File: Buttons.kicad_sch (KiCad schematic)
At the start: 0 parts

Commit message: added buttons schematic
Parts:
- added C27, C28, C29, C30, C31, C32, C33, C34: 100nF, 0_capacitors:C_0402_1005Metric, symbol 0_capacitors:CL05B104KO5NNNC
- added R20, R23, R25, R27, R29, R31, R33, R35: 47kΩ, 0_resistors:R_0402_1005Metric, symbol 0_resistors:0402WGF4702TCE
- added R21, R22, R24, R26, R28, R30, R32, R34: 5.1kΩ, 0_resistors:R_0402_1005Metric, symbol 0_resistors:0402WGF5101TCE
- added S1, S2: SKRTLAE010, 0_switches:SKRTLAE010, symbol 0_switches:SKRTLAE010
- added SW1, SW2, SW3, SW4, SW5, SW6: Button SPST SMD Tactile Switch, 0_switches:SW_TS-1088-AR02016, symbol 0_switches:SW_Push
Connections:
- new net: C31.1, R28.2, R29.2, SW5.1
- new net: C33.1, R32.2, R33.2, S1.2
- new net: C34.1, R34.2, R35.2, S2.2
- new net: C32.1, R30.2, R31.2, SW6.1
- new net: C29.1, R24.2, R25.2, SW3.1
- new net: C27.1, R20.2, R21.2, SW1.2
- new net: C28.1, R22.2, R23.2, SW2.1
- new net: C30.1, R26.2, R27.2, SW4.1
- new net +3.3V: R20.1, R23.1, R25.1, R27.1, R29.1, R31.1, R33.1, R35.1
- new net BUTTON1: R21.1
- new net BUTTON2: R22.1
- new net BUTTON3: R24.1
- new net BUTTON4: R26.1
- new net BUTTON5: R28.1
- new net BUTTON6: R30.1
- new net BUTTON7: R32.1
- new net BUTTON8: R34.1
- new net GND: C27.2, C28.2, C29.2, C30.2, C31.2, C32.2, C33.2, C34.2, S1.1, S1.3, S2.1, S2.3, SW1.1, SW2.2, SW3.2, SW4.2, SW5.2, SW6.2
- no-connect marks 0 -> 4
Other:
- title: (none) -> UI - Buttons

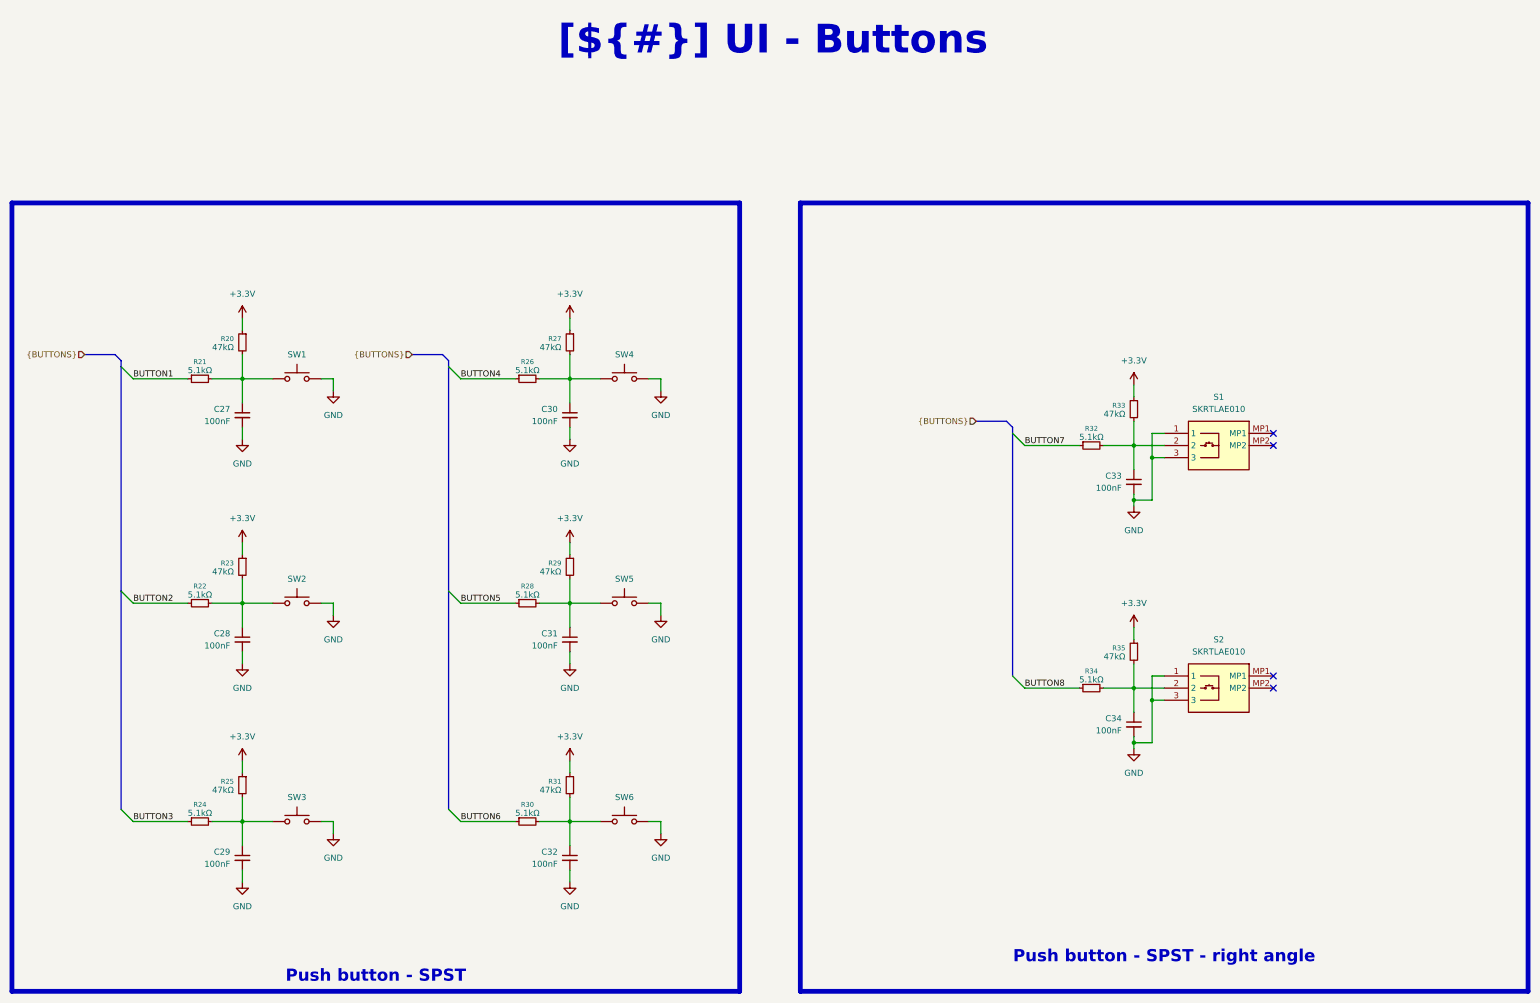
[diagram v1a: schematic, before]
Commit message: 3 pos toggle switch input
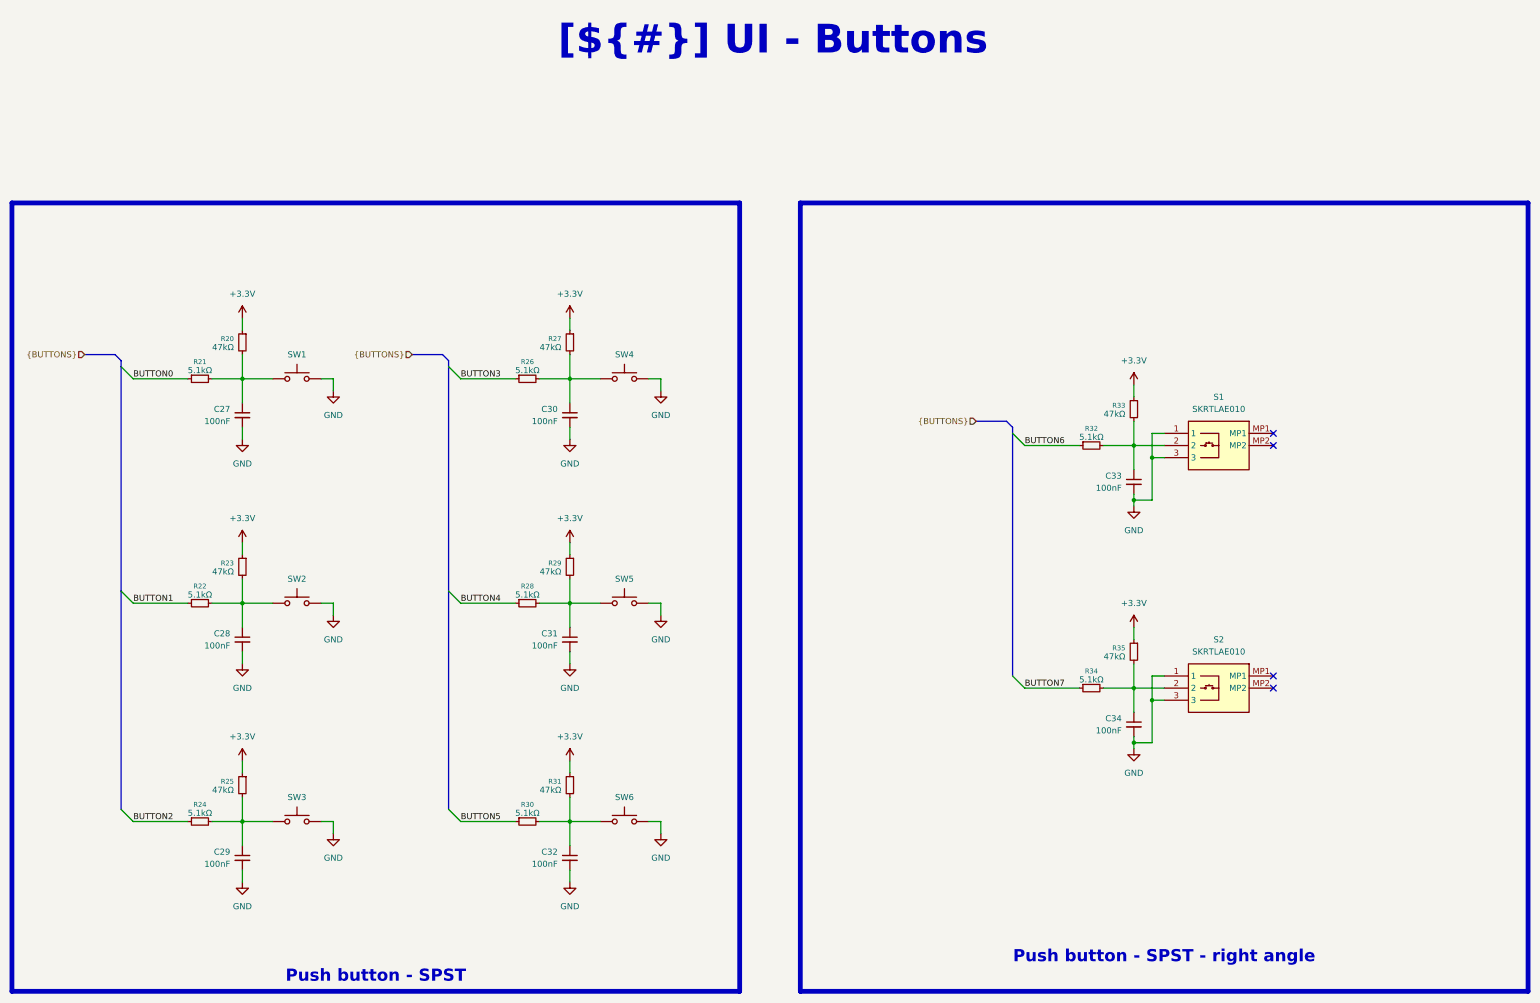
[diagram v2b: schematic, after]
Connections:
- net BUTTON8 is gone; now on net BUTTON7: R34.1
- net BUTTON1: now also R22.1; no longer R21.1
- net BUTTON2: now also R24.1; no longer R22.1
- net BUTTON3: now also R26.1; no longer R24.1
- net BUTTON4: now also R28.1; no longer R26.1
- net BUTTON5: now also R30.1; no longer R28.1
- net BUTTON6: now also R32.1; no longer R30.1
- net BUTTON7: no longer R32.1
- new net BUTTON0: R21.1
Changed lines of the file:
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@@
 	)
 	(bus_alias "BUTTONS"
-		(members "BUTTON[1..8]")
+		(members "BUTTON[0..7]" "TOGGLE[0..1]")
 	)
 	(rectangle
@@
 		)
 	)
-	(label "BUTTON8"
+	(label "BUTTON7"
 		(at 262.89 154.94 0)
 		(effects
@@
 		)
 	)
-	(label "BUTTON6"
+	(label "BUTTON5"
 		(at 144.78 182.88 0)
 		(effects
@@
 		)
 	)
-	(label "BUTTON2"
+	(label "BUTTON1"
 		(at 76.2 137.16 0)
 		(effects
@@
 		)
 	)
-	(label "BUTTON7"
+	(label "BUTTON6"
 		(at 262.89 104.14 0)
 		(effects
@@
 		)
 	)
-	(label "BUTTON1"
+	(label "BUTTON0"
 		(at 76.2 90.17 0)
 		(effects
@@
 		)
 	)
-	(label "BUTTON4"
+	(label "BUTTON3"
 		(at 144.78 90.17 0)
 		(effects
@@
 		)
 	)
-	(label "BUTTON5"
+	(label "BUTTON4"
 		(at 144.78 137.16 0)
 		(effects
@@
 		)
 	)
-	(label "BUTTON3"
+	(label "BUTTON2"
 		(at 76.2 182.88 0)
 		(effects

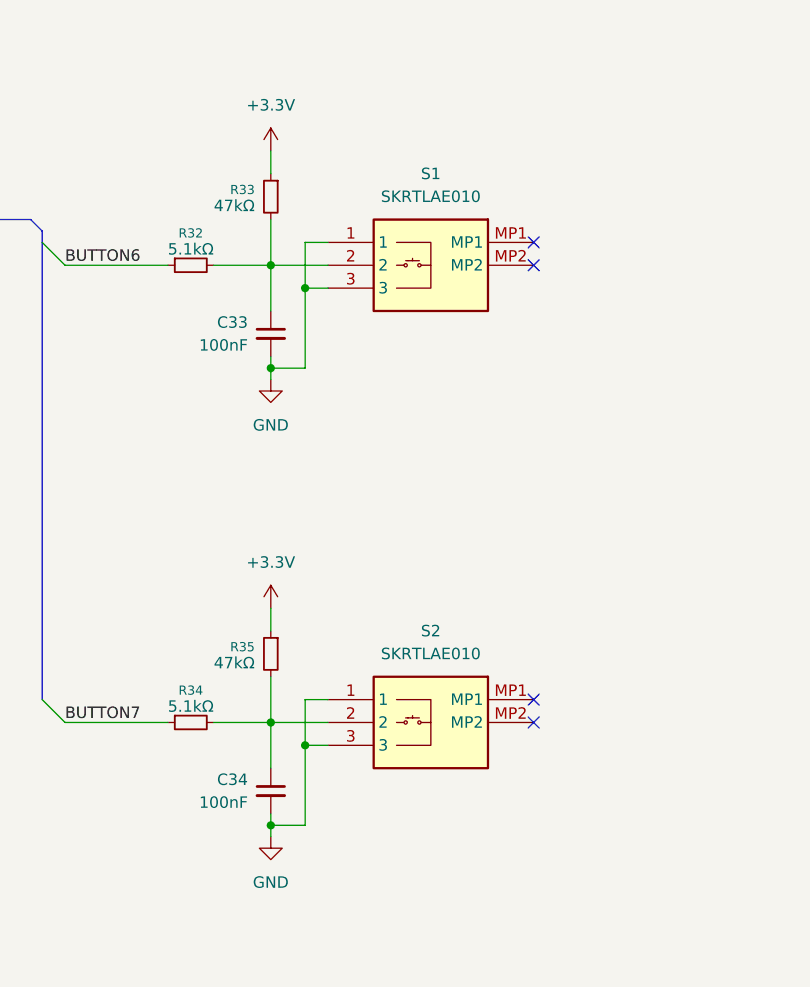
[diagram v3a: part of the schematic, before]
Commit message: change buttons footprints to 2pin 2.0mm connectors
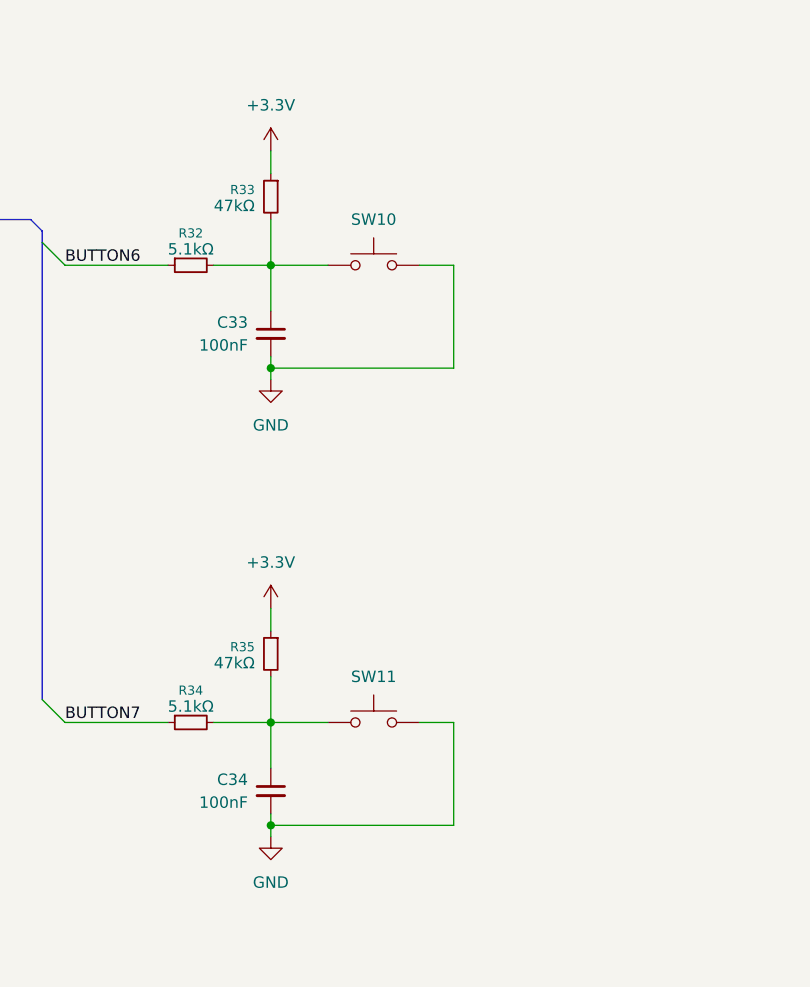
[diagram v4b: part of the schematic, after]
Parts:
- removed S1, S2: SKRTLAE010, 0_switches:SKRTLAE010, symbol 0_switches:SKRTLAE010
- added SW10, SW11: Button SPST SMD Tactile Switch, Connector_JST:JST_PH_B2B-PH-K_1x02_P2.00mm_Vertical, symbol 0_switches:SW_Push
- SW1, SW2, SW3, SW4, SW5, SW6: footprint 0_switches:SW_TS-1088-AR02016 -> Connector_JST:JST_PH_B2B-PH-K_1x02_P2.00mm_Vertical; Supplier Part Number 1 C720477 -> C131337
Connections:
- net GND: now also SW10.2, SW11.2
- net at C33.1, R32.2, R33.2: now also SW10.1
- net at C34.1, R34.2, R35.2: now also SW11.1
- no-connect marks 4 -> 0

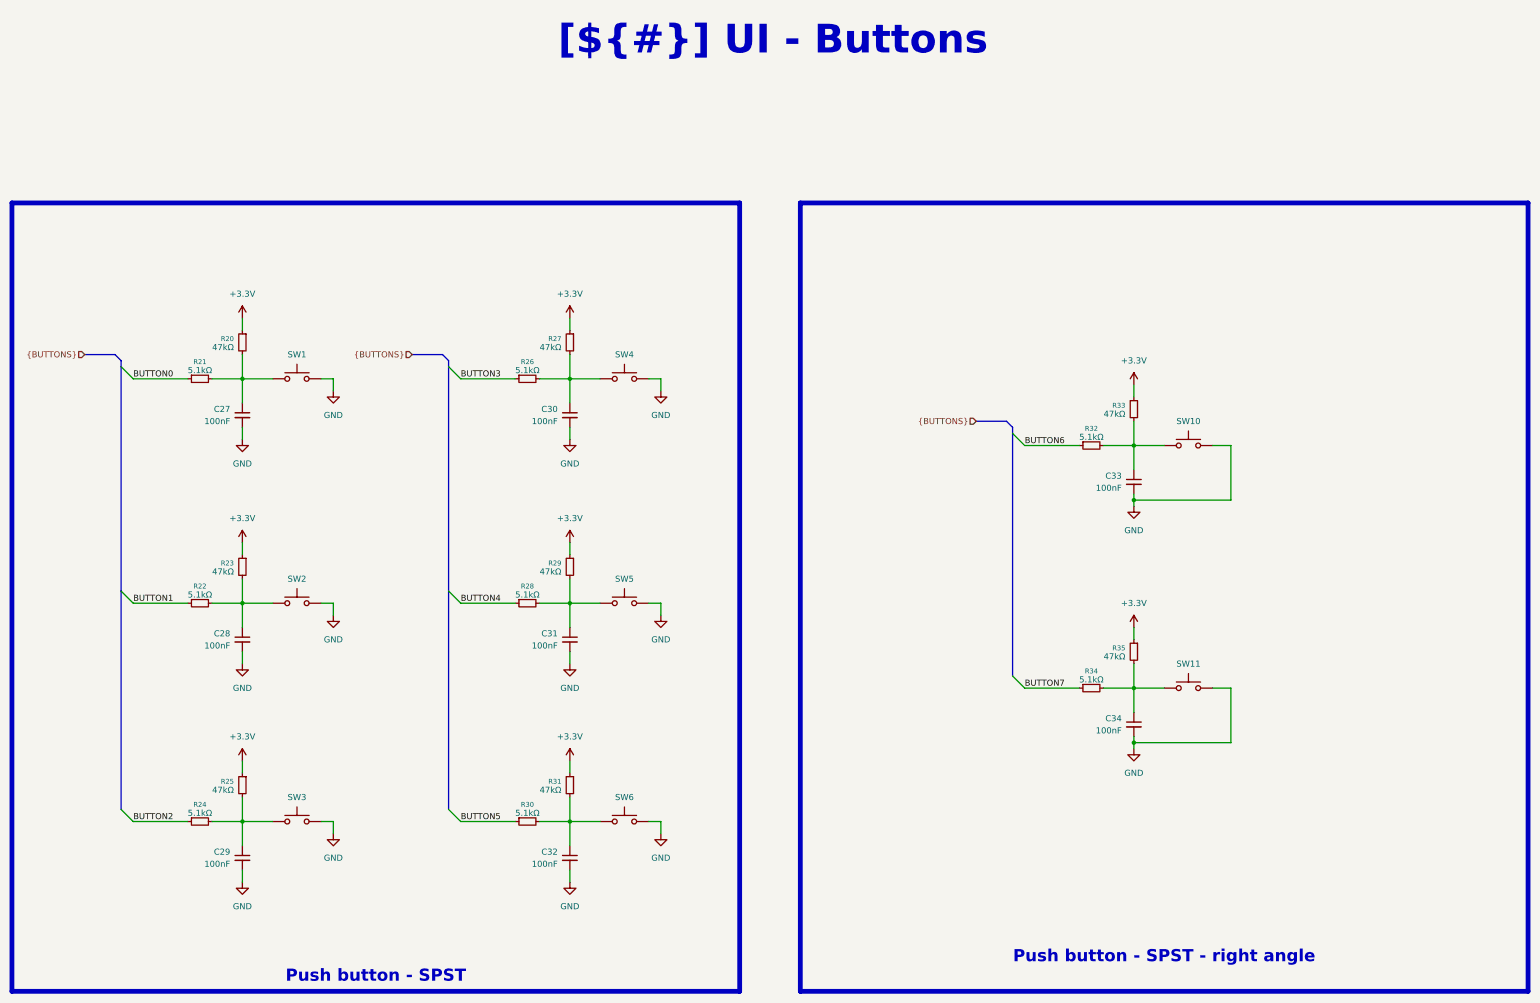
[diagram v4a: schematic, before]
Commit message: added tvs diodes to protect inputs + final component placement
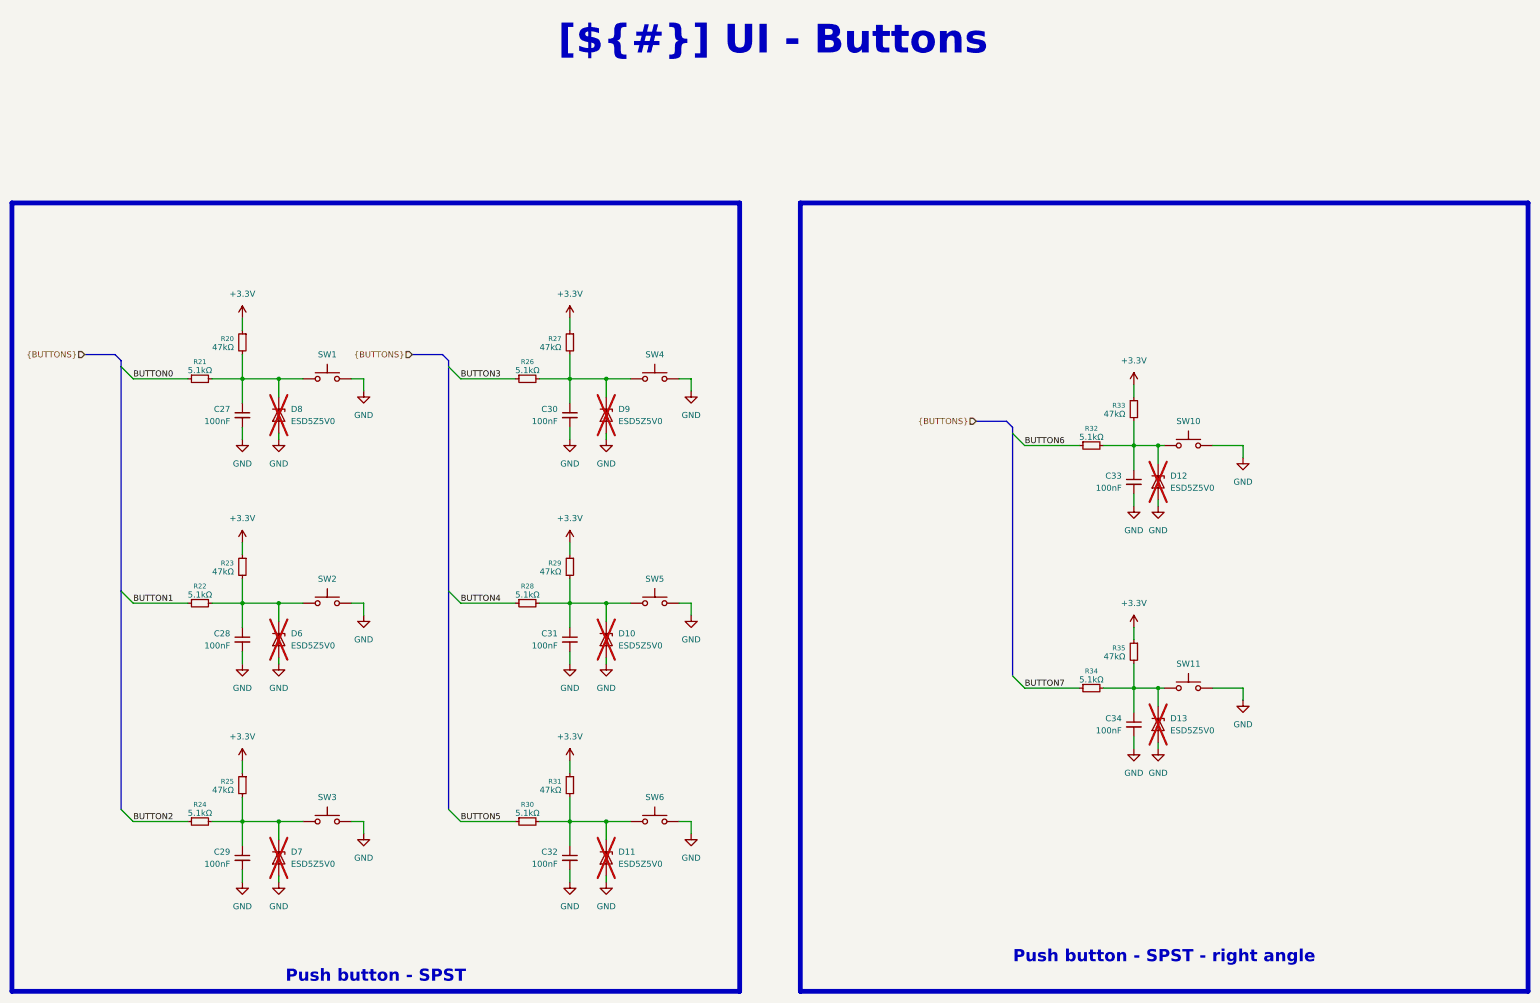
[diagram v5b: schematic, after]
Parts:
- added D10, D11, D12, D13, D6, D7, D8, D9: ESD5Z5V0, 0_diodes:D_SOD-523, symbol 0_diodes:ESD5Z5V0
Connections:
- net GND: now also SW1.2, D10.2 (A), D11.2 (A), D12.2 (A), D13.2 (A), D6.2 (A), D7.2 (A), D8.2 (A), D9.2 (A); no longer SW1.1
- net at C31.1, R28.2, R29.2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: now also D10.1 (K)
- net at C33.1, R32.2, R33.2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: now also D12.1 (K)
- net at C34.1, R34.2, R35.2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: now also D13.1 (K)
- net at C32.1, R30.2, R31.2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: now also D11.1 (K)
- net at C29.1, R24.2, R25.2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: now also D7.1 (K)
- net at C27.1, R20.2, R21.2: now also SW1.1, D8.1 (K); no longer SW1.2
- net at C28.1, R22.2, R23.2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: now also D6.1 (K)
- net at C30.1, R26.2, R27.2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: now also D9.1 (K)
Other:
- moved on the sheet: SW1, SW2, SW3, SW4, SW5, SW6

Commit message: designator chagnes and cleanup silkscreen
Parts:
- C27, C28, C29, C30, C31, C32, C33, C34: LCSC PN (none) -> C1525
- D10, D11, D12, D13, D6, D7, D8, D9: LCSC PN (none) -> C191023
- R20, R23, R25, R27, R29, R31, R33, R35: LCSC PN (none) -> C25792
- R21, R22, R24, R26, R28, R30, R32, R34: LCSC PN (none) -> C25905
- SW1, SW10, SW11, SW2, SW3, SW4, SW5, SW6: LCSC PN (none) -> C720477; Supplier Part Number 1 C131337 -> C720477
